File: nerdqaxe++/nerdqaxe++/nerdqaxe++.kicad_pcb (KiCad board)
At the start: 6 copper layers, 89 x 165 mm, 238 parts, among them J1 5.5mm/8A, J2 Conn_01x06, M1 Fan_4pin, M2 Fan_4pin, U10 CSD95472Q5MC, U19 BM1370_mode1, U20 BM1370_mode1, U25 BM1370_mode1, U26 BM1370_mode1, U3 TPS53647, U30 T-Display-S3, U32 EMC2302-1, U33 TXU0102-DCU, U35 TXU0304PW, U36 MCP1824T-1202E, U37 TMP1075, U38 TMP1075, U4 CSD95472Q5MC, U6 AP3211, U7 MCP1824T-0802E, U8 25MHz, U9 CSD95472Q5MC

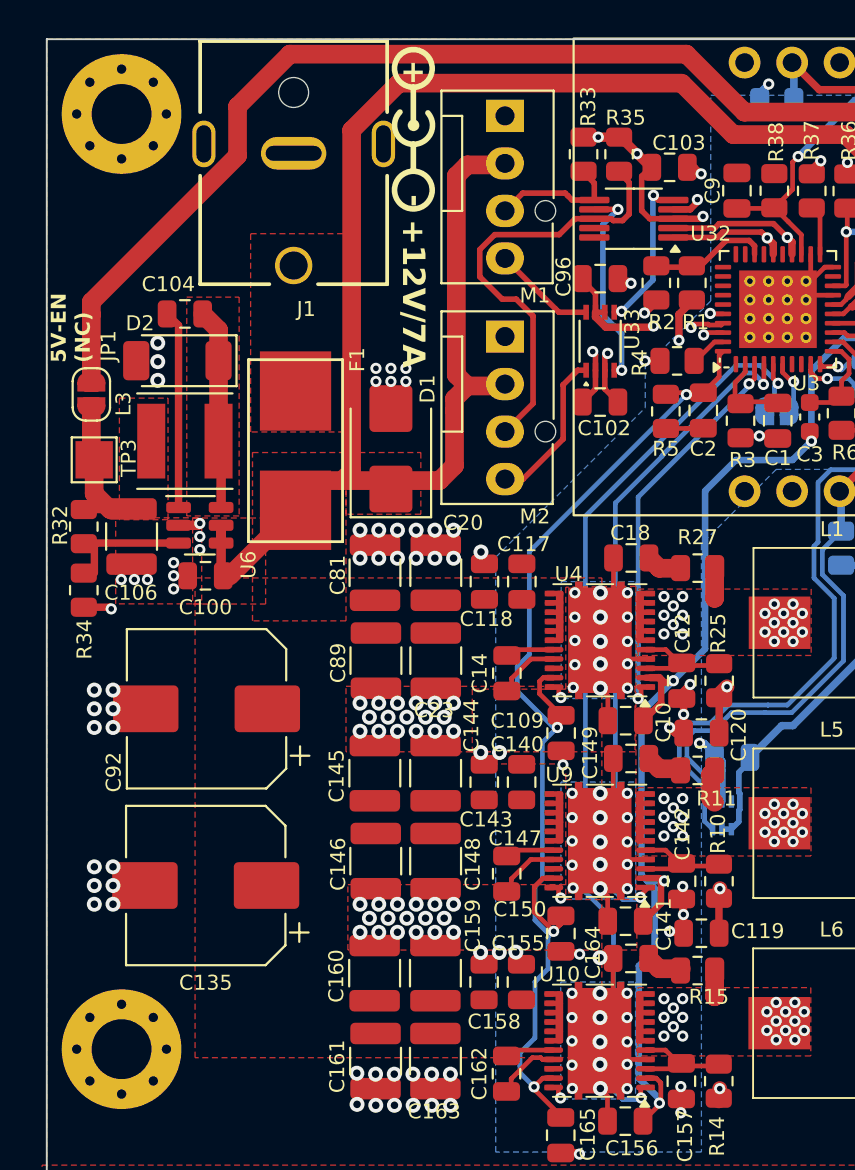
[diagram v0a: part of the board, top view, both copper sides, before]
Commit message: Updated PCB layout
- Replaced barrel jack socket with XT30M
- Replaced old fuse holder with new 3568
- Reordered components for AP3211 5V buck converter
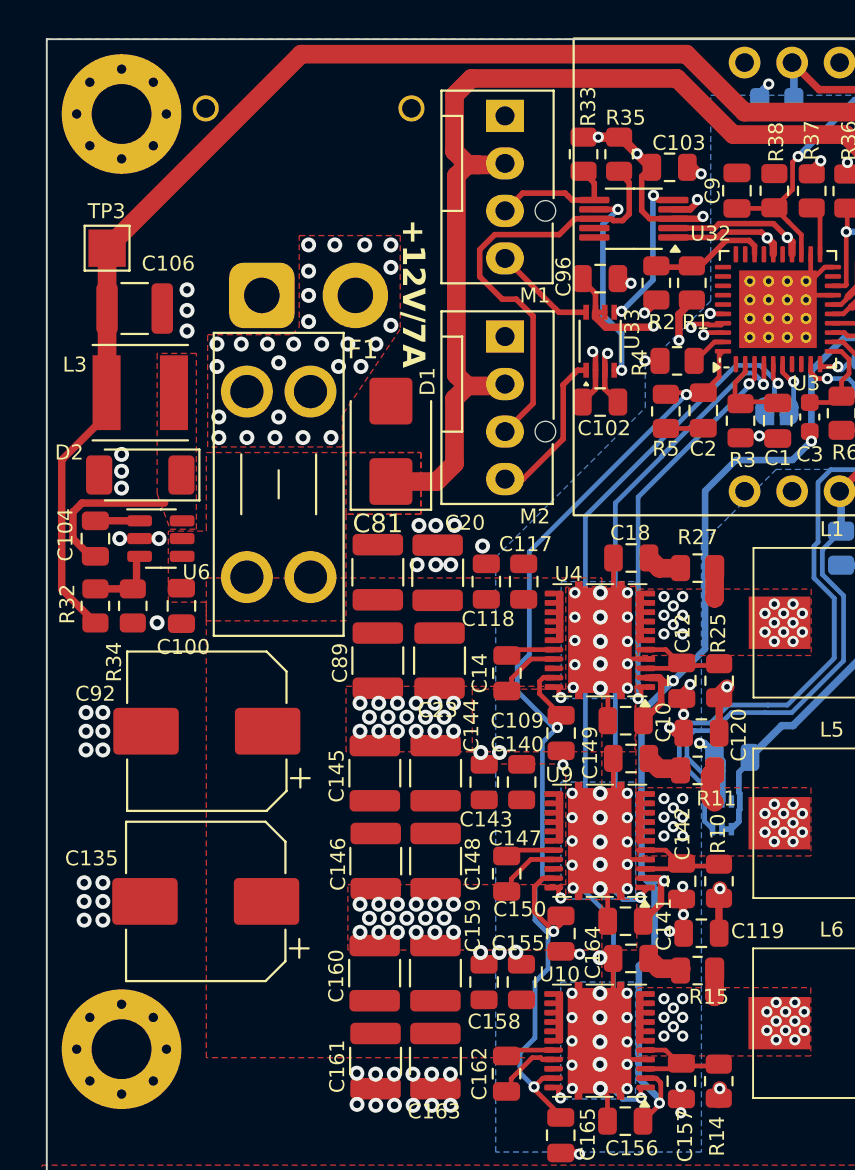
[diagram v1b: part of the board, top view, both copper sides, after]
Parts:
- removed JP1: SolderJumper_2_Open, Jumper:SolderJumper-2_P1.3mm_Open_RoundedPad1.0x1.5mm
- removed U1: ~, qaxe:polarity
- F1: footprint myfootprints:fuseholder_littlefuse_blok -> Fuse:Fuseholder_Blade_Mini_Keystone_3568
- J1: value 5.5mm/8A -> XT30; footprint qaxe:GCT_DCJ250-20-B-XX-X_REVA1 -> Connector_AMASS:AMASS_XT30PW-M_1x02_P2.50mm_Horizontal; moved to B.Cu
- moved C104 12.9 mm to (53.6, 50.7), turned to -90 degrees
- moved C106 12.2 mm to (55.7, 38.4), turned to 0 degrees
- moved TP3 11.3 mm to (54.2, 35.2)
- moved J1 7.30 mm to (62.5, 37.7)
- moved F1 7.24 mm to (61.7, 52.8)
- moved D2 6.42 mm to (56.0, 47.3)
- moved R32 4.29 mm to (53.6, 54.3), turned to 90 degrees
- moved L3 3.52 mm to (56.0, 42.9)
- moved R34 2.75 mm to (55.6, 54.3)
- moved U6 2.20 mm to (57.1, 50.7)
- moved C100 2.06 mm to (58.2, 54.3), turned to -90 degrees
- moved C92 1.20 mm to (59.6, 61.0)
- moved C135 0.85 mm to (59.5, 70.1)
- moved D1 0.40 mm to (69.4, 45.5)
- moved C23 0.20 mm to (72.0, 57.2)
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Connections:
- net /BM1366/BI renamed /BM1370/BI
- net /BM1366/CI renamed /BM1370/CI
- net /BM1366/CLKI renamed /BM1370/CLKI
- net /BM1366/RESET renamed /BM1370/RESET
- net /BM1366/RO renamed /BM1370/RO
- net /BM1366/RST_N renamed /BM1370/RST_N
- net /BM1366/RXD renamed /BM1370/RXD
- net /BM1366/TXD renamed /BM1370/TXD
- C106 pad 1: Net-(JP1-A) -> +5V
- F1 pad 2: Net-(F1-Pad2) -> Net-(J1-Pin_2)
- J1 pad 1: Net-(F1-Pad2) -> GND
- J1 pad 2: GND -> Net-(J1-Pin_2)
- L3 pad 2: Net-(JP1-A) -> +5V
- R32 pad 1: Net-(JP1-A) -> +5V
- TP3 pad 1: Net-(JP1-A) -> +5V
- U3 pad 33: (no net) -> unconnected-(U3-NC-Pad33)
- U3 pad 34: (no net) -> unconnected-(U3-NC-Pad34)
- U3 pad 7: (no net) -> unconnected-(U3-NC-Pad7)
- U3 pad 8: (no net) -> unconnected-(U3-NC-Pad8)
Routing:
- net +12V: track 90.7 -> 54.7 mm
- net +5V: track 151.7 -> 165.6 mm
- net Net-(JP1-A): track 9.34 -> 0.00 mm
- net Net-(U6-BS): track 10.6 -> 2.59 mm
- net Net-(D2-K): track 10.8 -> 8.11 mm
- net GND: track 184.4 -> 182.3 mm, vias 445 -> 429
- net Net-(U6-FB): track 6.09 -> 4.08 mm
- net Net-(J1-Pin_2): vias 0 -> 27
- added copper zone on F.Cu, net Net-(J1-Pin_2)
- added copper zone on In1.Cu, net Net-(J1-Pin_2)
- added copper zone on In2.Cu, net Net-(J1-Pin_2)
- removed copper zone on F.Cu, net Net-(F1-Pad2)
- removed copper zone on F.Cu, net Net-(JP1-A)
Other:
- board text removed: "5V-EN (NC)"

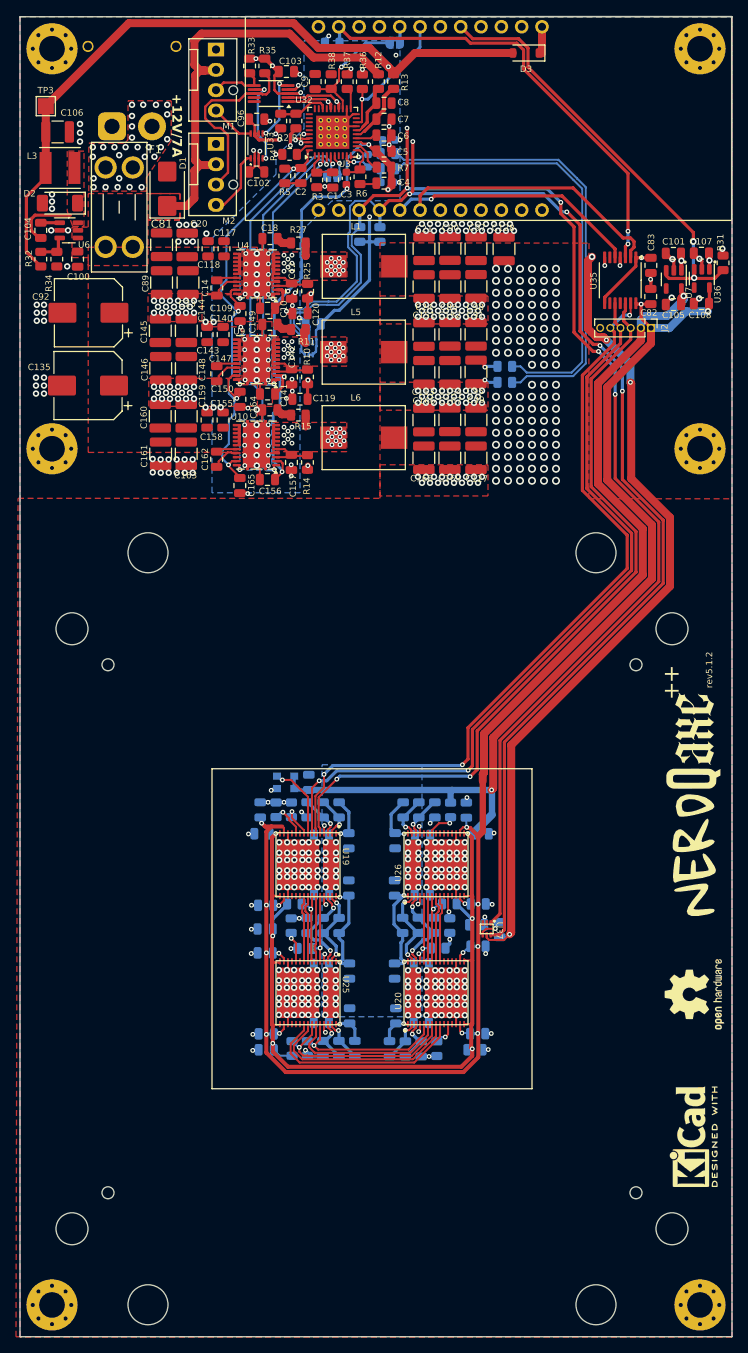
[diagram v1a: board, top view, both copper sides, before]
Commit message: Nerdqaxe++ rev6.1.2PM
1. BM1370 Footprint solder paste revision
2. Added 2R2 resistor in series with bootstrap cap for CSD95472Q5MC
3. 180nH inductors for CSD
4. Vsense closer to ASICs
5. Fiducials
6. Updated top silkscreen
7. Various changes in tracing
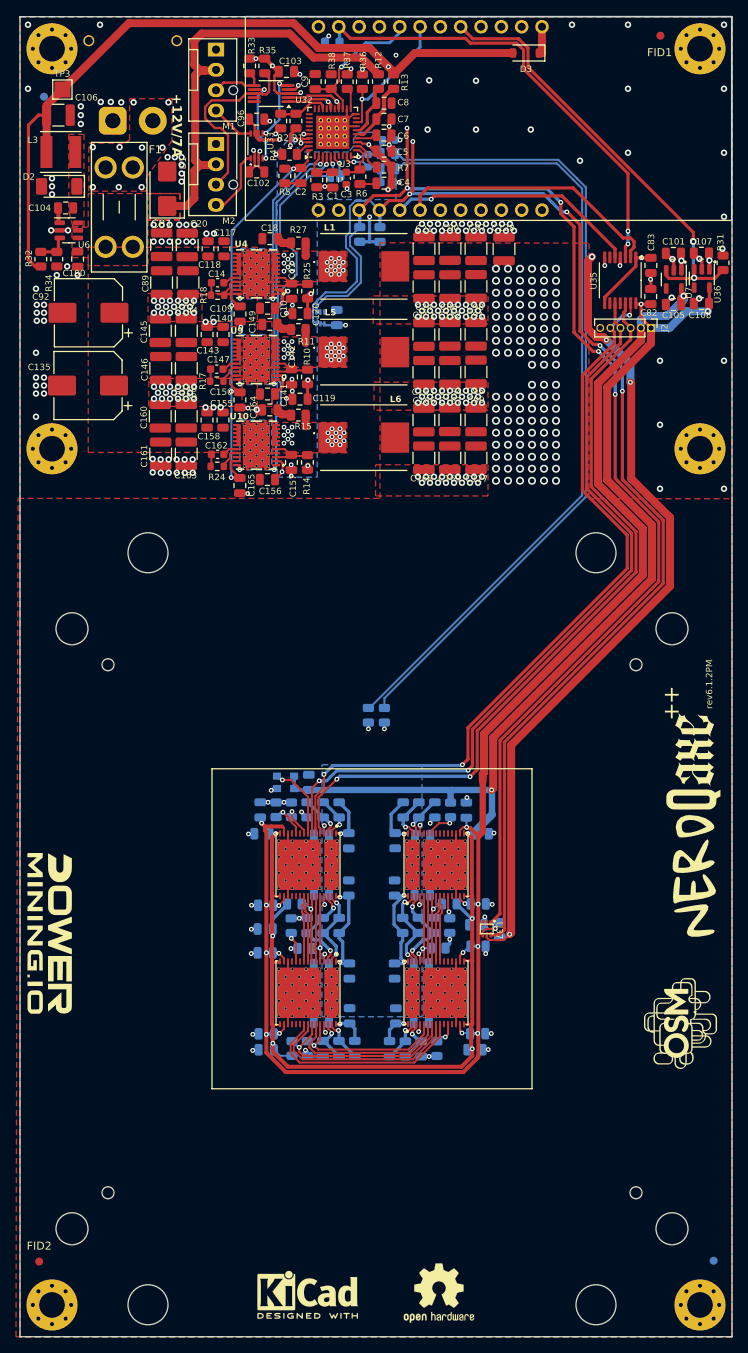
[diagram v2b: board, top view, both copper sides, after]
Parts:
- removed JP2: SolderJumper_2_Open, Jumper:SolderJumper-2_P1.3mm_Open_RoundedPad1.0x1.5mm
- added ?: LOGO, LOGO, F.Cu at (54.6, 137.6)
- added FID1: Fiducial, Fiducial:Fiducial_1mm_Mask2mm, F.Cu at (131.1, 26.4)
- added FID2: Fiducial, Fiducial:Fiducial_1mm_Mask2mm, F.Cu at (53.4, 179.6)
- added FID3: Fiducial, Fiducial:Fiducial_1mm_Mask2mm, B.Cu at (137.7, 179.5)
- added FID4: Fiducial, Fiducial:Fiducial_1mm_Mask2mm, B.Cu at (54.0, 34.0)
- added G***: LOGO, LOGO, F.Cu at (133.8, 149.8)
- added R17: 2.2R, Resistor_SMD:R_0603_1608Metric, F.Cu at (75.6, 69.5)
- added R18: 2.2R, Resistor_SMD:R_0603_1608Metric, F.Cu at (75.7, 58.8)
- added R24: 2.2R, Resistor_SMD:R_0603_1608Metric, F.Cu at (75.7, 80.2)
- C14, C147, C162: footprint Capacitor_SMD:C_0805_2012Metric -> Capacitor_SMD:C_0603_1608Metric
- L1, L5, L6: value 220nH -> 180nH; footprint myfootprints:IFLR-4031GC-01-8x10 -> qaxe:PA5187181HLT
- U10, U4, U9: footprint myfootprints:CSD95472-SON-5x6 -> qaxe:CSD95472Q5MC
- U19, U20, U25, U26: footprint myfootprints:BM1370 -> qaxe:BM1370_JB
- moved REF** 52.1 mm to (87.0, 183.8), turned to 0 degrees
- moved REF** 49.1 mm to (103.4, 183.5), turned to 0 degrees
- moved R29 46.8 mm to (94.5, 111.3), turned to -90 degrees
- moved R30 44.3 mm to (96.5, 111.3), turned to -90 degrees
- moved REF** 9.50 mm to (123.0, 185.0)
- moved REF** 9.50 mm to (67.0, 91.0)
- moved REF** 9.50 mm to (67.0, 185.0)
- moved C104 4.18 mm to (56.7, 47.9), turned to 0 degrees
- moved U38 4.11 mm to (88.5, 61.6)
- moved C87 3.06 mm to (90.6, 61.6), turned to 90 degrees
- moved TP3 2.93 mm to (56.3, 33.1)
- moved G*** 2.60 mm to (135.2, 117.1)
- moved G*** 2.60 mm to (135.2, 131.5)
- moved C106 2.10 mm to (55.8, 36.3)
- moved D2 2.10 mm to (55.9, 45.2)
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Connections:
- C14 pad 1: Net-(U4-BOOT) -> Net-(C14-Pad1)
- C147 pad 1: Net-(U9-BOOT) -> Net-(C147-Pad1)
- C162 pad 1: Net-(U10-BOOT) -> Net-(C162-Pad1)
- C9 pad 1: Net-(JP2-A) -> /Power/PWR_EN
- R38 pad 1: Net-(JP2-A) -> /Power/PWR_EN
- U3 pad 23: Net-(JP2-A) -> /Power/PWR_EN
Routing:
- net +VRef: track 73.8 -> 23.7 mm
- net /Power/VSENSE+: track 56.4 -> 101.2 mm
- net GND: track 182.3 -> 138.2 mm, vias 429 -> 281
- net /Power/VSENSE-: track 58.0 -> 101.3 mm
- net /Power/PWR_EN: track 2.04 -> 18.2 mm, vias 0 -> 1
- net Net-(JP2-A): track 15.8 -> 0.00 mm, vias 1 -> 0
- net Net-(D2-K): track 8.11 -> 0.00 mm
- net /T-Display-S3/SCL: track 180.5 -> 174.2 mm
- net /T-Display-S3/SDA: track 188.5 -> 182.2 mm
- net +5V: track 165.6 -> 171.0 mm
- net +3V3: track 157.7 -> 161.9 mm, vias 15 -> 16
- net /Power/TPS_CSP3: track 50.6 -> 46.6 mm
- net /Power/TPS_CSP2: track 35.9 -> 33.7 mm
- net Net-(C14-Pad1): track 0.00 -> 1.64 mm
- net Net-(U3-V5): track 10.3 -> 8.73 mm
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- removed copper zone on In4.Cu, net Net-(U10-VSW)
- removed copper zone on In4.Cu, net Net-(U4-VSW)
- removed copper zone on In4.Cu, net Net-(U9-VSW)
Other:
- board text added: "rev6.1.2PM"
- board text removed: "TPS-EN (NC)"
- board text removed: "rev5.1.2"
